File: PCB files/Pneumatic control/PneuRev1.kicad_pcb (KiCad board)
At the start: 2 copper layers, 145.7 x 92.9 mm, 52 parts, among them J1 SIG_IN, J2 BATT_IN, J3 PNEU, U1 uA7824, U2 OP279, U3 OP279, U4 OP279, U5 OP279, U6 OP279, U7 OP279, U8 OP07

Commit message: 2/4/2019
-Finished board routing
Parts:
- moved J2 74.6 mm to (162.6, 68.8), turned to 0 degrees
- moved R40 63.4 mm to (157.7, 71.6), turned to 90 degrees
- moved D1 50.2 mm to (152.8, 69.5)
- moved R39 38.4 mm to (105.4, 72.0)
- moved R38 32.1 mm to (105.4, 76.4), turned to 270 degrees
- moved R19 30.1 mm to (111.6, 131.9), turned to 0 degrees
- moved U8 28.6 mm to (118.1, 77.1)
- moved R37 28.0 mm to (110.6, 82.9)
- moved R21 25.2 mm to (146.4, 132.7), turned to 0 degrees
- moved R1 22.8 mm to (111.1, 107.8)
- moved R24 21.7 mm to (140.7, 125.3), turned to 270 degrees
- moved R29 20.9 mm to (181.9, 132.1), turned to 0 degrees
- moved R11 20.8 mm to (182.7, 106.5)
- moved R3 20.8 mm to (146.1, 106.7)
- moved R22 19.9 mm to (106.8, 125.6)
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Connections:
- U2 pad 1: Net-(J1-Pad1) -> /PNU1
- U2 pad 2: GND -> Net-(R4-Pad1)
- U2 pad 3: /IN2 -> Net-(J1-Pad1)
- U2 pad 4: Net-(R5-Pad1) -> GND
- U2 pad 5: /PNU2 -> /IN2
- U2 pad 6: Net-(U1-Pad3) -> Net-(R5-Pad1)
- U2 pad 7: /PNU1 -> /PNU2
- U2 pad 8: Net-(R4-Pad1) -> Net-(U1-Pad3)
- U3 pad 1: /IN3 -> /PNU3
- U3 pad 2: GND -> Net-(R6-Pad1)
- U3 pad 3: /IN4 -> /IN3
- U3 pad 4: Net-(R13-Pad1) -> GND
- U3 pad 5: /PNU4 -> /IN4
- U3 pad 6: Net-(U1-Pad3) -> Net-(R13-Pad1)
- U3 pad 7: /PNU3 -> /PNU4
- U3 pad 8: Net-(R6-Pad1) -> Net-(U1-Pad3)
- U4 pad 1: /IN5 -> /PNU5
- U4 pad 2: GND -> Net-(R14-Pad1)
- U4 pad 3: /IN6 -> /IN5
- U4 pad 4: Net-(R15-Pad1) -> GND
- U4 pad 5: /PNU6 -> /IN6
- U4 pad 6: Net-(U2-Pad6) -> Net-(R15-Pad1)
- U4 pad 7: /PNU5 -> /PNU6
- U4 pad 8: Net-(R14-Pad1) -> Net-(U1-Pad3)
- U5 pad 1: /IN7 -> /PNU7
- U5 pad 2: GND -> Net-(R22-Pad1)
- U5 pad 3: /IN8 -> /IN7
- U5 pad 4: Net-(R23-Pad1) -> GND
- U5 pad 5: /PNU8 -> /IN8
- U5 pad 6: Net-(U1-Pad3) -> Net-(R23-Pad1)
- U5 pad 7: /PNU7 -> /PNU8
- U5 pad 8: Net-(R22-Pad1) -> Net-(U1-Pad3)
- U6 pad 1: /IN9 -> /PNU9
- U6 pad 2: GND -> Net-(R24-Pad1)
- U6 pad 3: /IN10 -> /IN9
- U6 pad 4: Net-(R31-Pad1) -> GND
- U6 pad 5: /PNU10 -> /IN10
- U6 pad 6: Net-(U1-Pad3) -> Net-(R31-Pad1)
- U6 pad 7: /PNU9 -> /PNU10
- U6 pad 8: Net-(R24-Pad1) -> Net-(U1-Pad3)
- U7 pad 1: /IN11 -> /PNU11
- U7 pad 2: GND -> Net-(R32-Pad1)
- U7 pad 3: /IN12 -> /IN11
- U7 pad 4: Net-(R33-Pad1) -> GND
- U7 pad 5: /PNU12 -> /IN12
- U7 pad 6: Net-(U2-Pad6) -> Net-(R33-Pad1)
- U7 pad 7: /PNU11 -> /PNU12
- U7 pad 8: Net-(R32-Pad1) -> Net-(U1-Pad3)
- U8 pad 1: /IN13 -> /PNU13
- U8 pad 2: GND -> Net-(R38-Pad1)
- U8 pad 3: Net-(U8-Pad3) -> /IN13
- U8 pad 4: Net-(U8-Pad4) -> GND
- U8 pad 6: Net-(U1-Pad3) -> Net-(U8-Pad6)
- U8 pad 7: /PNU13 -> Net-(U8-Pad7)
- U8 pad 8: Net-(R38-Pad1) -> Net-(U1-Pad3)
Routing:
- net Net-(U1-Pad3): track 0.00 -> 249.5 mm, vias 0 -> 10
- net /IN6: track 0.00 -> 136.3 mm, vias 0 -> 4
- net /IN12: track 0.00 -> 135.3 mm, vias 0 -> 2
- net /PNU7: track 0.00 -> 130.8 mm, vias 0 -> 4
- net /PNU1: track 0.00 -> 127.3 mm, vias 0 -> 2
- net /PNU8: track 0.00 -> 123.8 mm, vias 0 -> 4
- net /IN11: track 0.00 -> 123.0 mm, vias 0 -> 2
- net /PNU2: track 0.00 -> 122.8 mm, vias 0 -> 4
- net /IN5: track 0.00 -> 122.3 mm, vias 0 -> 3
- net /PNU13: track 0.00 -> 116.6 mm, vias 0 -> 2
- net /PNU5: track 0.00 -> 104.8 mm, vias 0 -> 2
- net /PNU9: track 0.00 -> 101.6 mm, vias 0 -> 4
- net /IN4: track 0.00 -> 98.6 mm, vias 0 -> 4
- net /IN10: track 0.00 -> 94.6 mm, vias 0 -> 4
- net /PNU10: track 0.00 -> 92.6 mm, vias 0 -> 4
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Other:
- board size 145.7 x 92.9 mm -> 135.4 x 77.3 mm

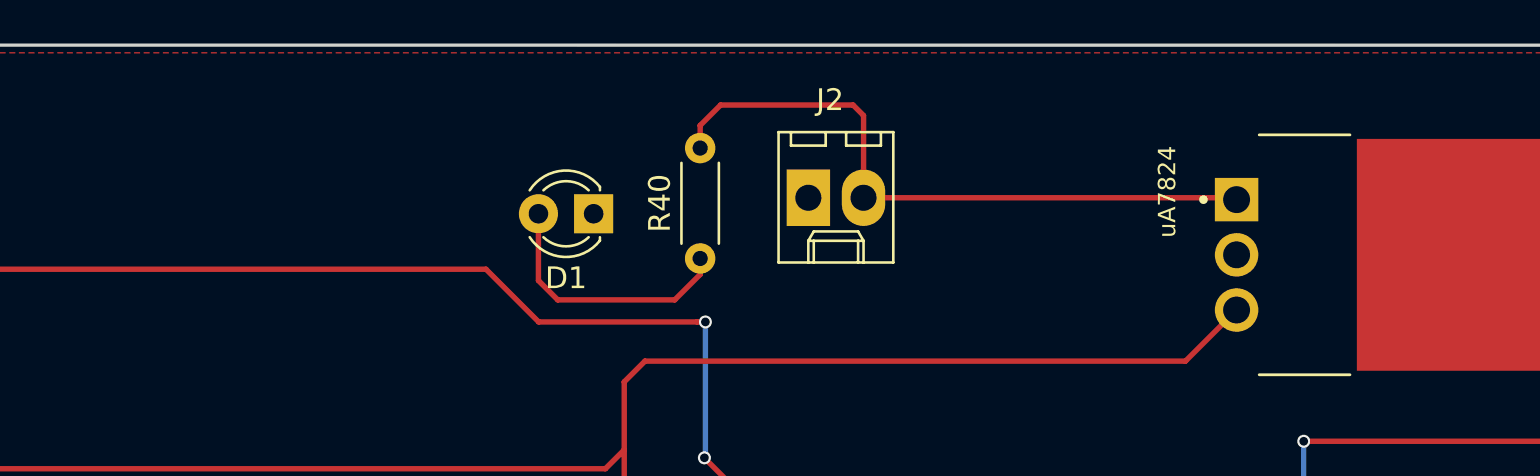
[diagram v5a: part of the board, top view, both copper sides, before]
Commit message: 2/10/2019
-Changed LED resistor to 1.5k
-Set BATT connector to a JST
-Found 383 ohm resistor to replace 390 ohm
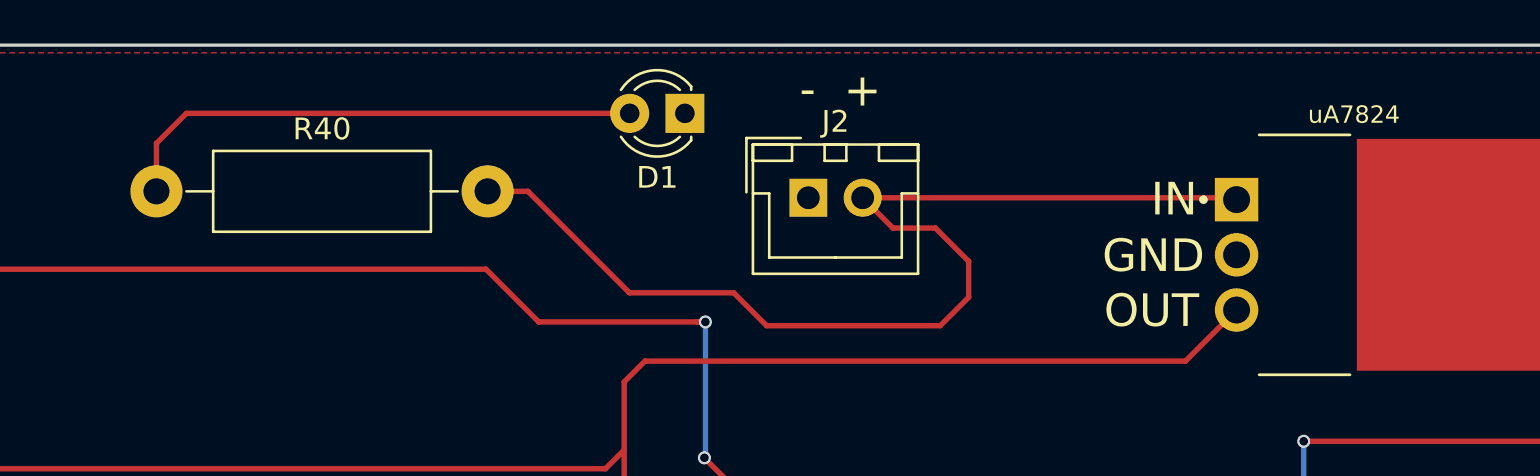
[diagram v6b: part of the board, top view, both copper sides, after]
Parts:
- J2: footprint Connectors_Molex:Molex_KK-6410-02_02x2.54mm_Straight -> Connectors_JST:JST_XH_B02B-XH-A_02x2.50mm_Straight
- R40: value 3k -> 1k5; footprint Resistors_THT:R_Axial_DIN0204_L3.6mm_D1.6mm_P5.08mm_Horizontal -> Resistors_THT:R_Axial_DIN0411_L9.9mm_D3.6mm_P15.24mm_Horizontal
- moved R40 25.2 mm to (132.6, 68.5), turned to 0 degrees
- moved D1 6.24 mm to (157.0, 64.9)
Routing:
- net Net-(J2-Pad2): track 30.9 -> 51.0 mm
- net Net-(D1-Pad2): track 12.1 -> 24.6 mm
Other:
- board text added: "+"
- board text added: "-"
- board text added: "GND"
- board text added: "IN"
- board text added: "OUT"

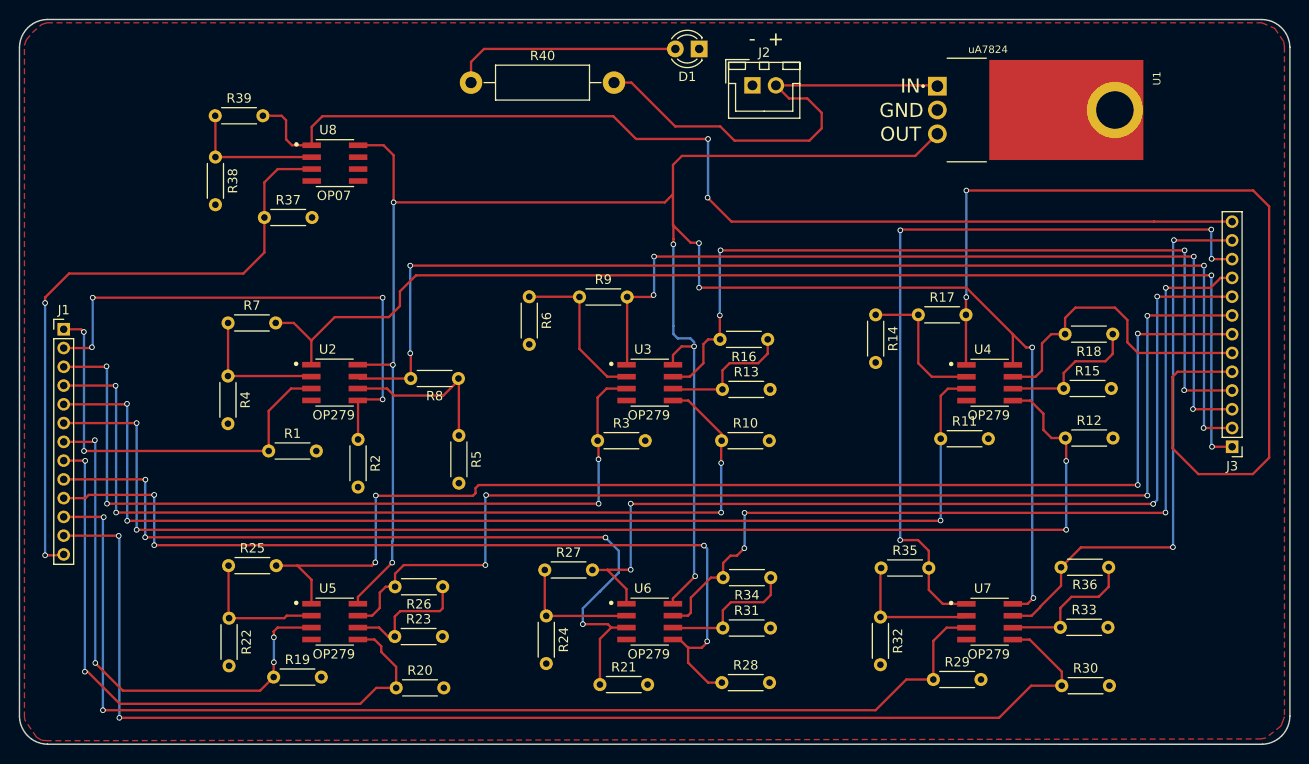
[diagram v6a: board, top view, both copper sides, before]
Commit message: 2/21/2019
-Selected capacitor footprint
-Generated netlist
-Began re-routing board
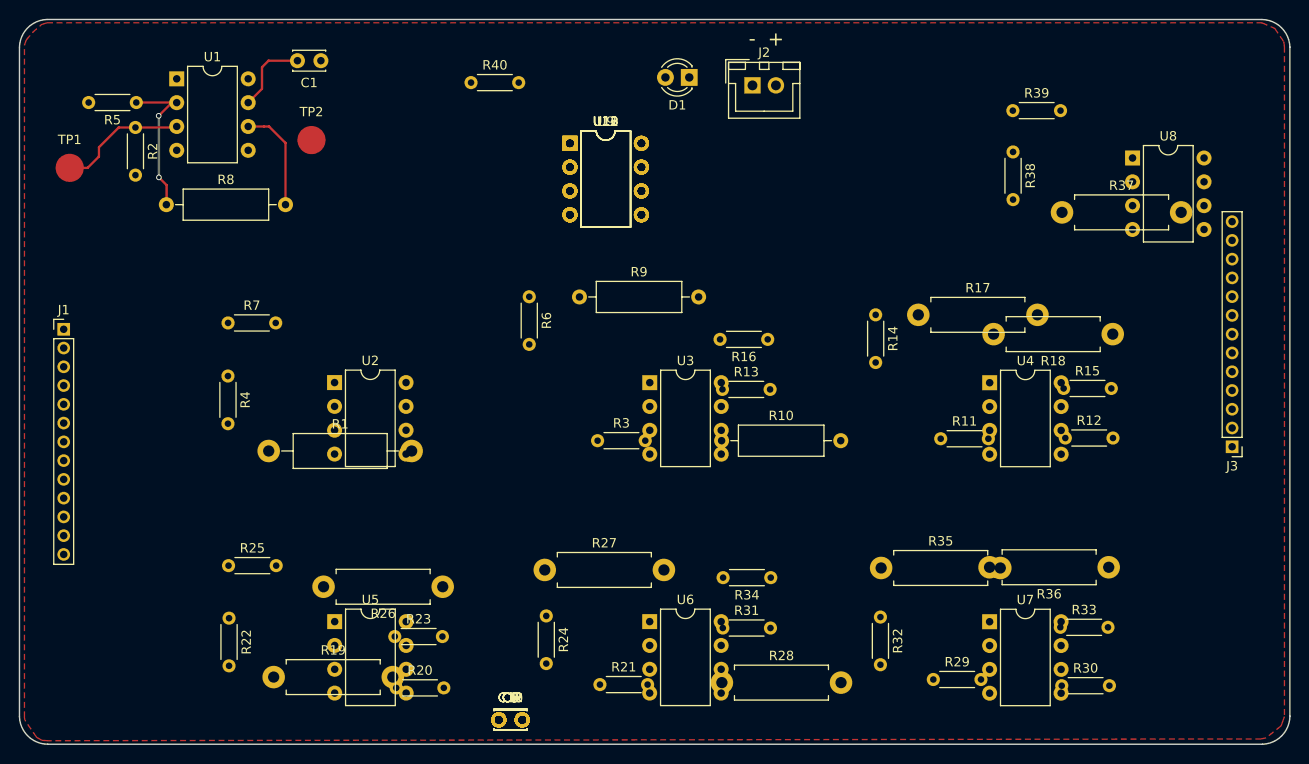
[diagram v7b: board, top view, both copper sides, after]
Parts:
- added C1: 1uF, Capacitors_THT:C_Disc_D3.4mm_W2.1mm_P2.50mm, F.Cu at (116.6, 66.2)
- added C10, C11, C12, C13, C2, C3, C4, C5, C6, C7, C8, C9: 1uF, Capacitors_THT:C_Disc_D3.4mm_W2.1mm_P2.50mm, F.Cu at (135.6, 136.4)
- added TP1: TEST, Measurement_Points:Measurement_Point_Round-SMD-Pad_Big, F.Cu at (89.9, 77.6)
- added TP2: TEST, Measurement_Points:Measurement_Point_Round-SMD-Pad_Big, F.Cu at (115.6, 74.6)
- added U10, U11, U12, U13, U9: OPA551, Housings_DIP:DIP-8_W7.62mm, F.Cu at (143.2, 75.0)
- R1: value 1k -> 3k; footprint Resistors_THT:R_Axial_DIN0204_L3.6mm_D1.6mm_P5.08mm_Horizontal -> Resistors_THT:R_Axial_DIN0411_L9.9mm_D3.6mm_P15.24mm_Horizontal
- R10: value 1k -> 4k; footprint Resistors_THT:R_Axial_DIN0204_L3.6mm_D1.6mm_P5.08mm_Horizontal -> Resistors_THT:R_Axial_DIN0309_L9.0mm_D3.2mm_P12.70mm_Horizontal
- R13, R14, R15, R22, R23, R24, R31, R32, R33, R38, R4, R5, R6: value 100 -> 1k
- R16, R25, R34, R39, R7: value 380 -> 1k
- R17, R18, R26, R27, R35, R36: value 380 -> 4k; footprint Resistors_THT:R_Axial_DIN0204_L3.6mm_D1.6mm_P5.08mm_Horizontal -> Resistors_THT:R_Axial_DIN0411_L9.9mm_D3.6mm_P12.70mm_Horizontal
- R19, R28, R37: value 1k -> 4k; footprint Resistors_THT:R_Axial_DIN0204_L3.6mm_D1.6mm_P5.08mm_Horizontal -> Resistors_THT:R_Axial_DIN0411_L9.9mm_D3.6mm_P12.70mm_Horizontal
- R40: value 1k5 -> 4k; footprint Resistors_THT:R_Axial_DIN0411_L9.9mm_D3.6mm_P15.24mm_Horizontal -> Resistors_THT:R_Axial_DIN0204_L3.6mm_D1.6mm_P5.08mm_Horizontal
- R8, R9: value 380 -> 4k; footprint Resistors_THT:R_Axial_DIN0204_L3.6mm_D1.6mm_P5.08mm_Horizontal -> Resistors_THT:R_Axial_DIN0309_L9.0mm_D3.2mm_P12.70mm_Horizontal
- U1: value uA7824 -> OPA551; footprint ua7824:TO254P1651X1067X470-3 -> Housings_DIP:DIP-8_W7.62mm
- U2, U3, U4, U5, U6, U7: value OP279 -> OPA551; footprint dualopamp:SOIC127P600X175-8N -> Housings_DIP:DIP-8_W7.62mm
- U8: value OP07 -> OPA551; footprint dualopamp:SOIC127P600X175-8N -> Housings_DIP:DIP-8_W7.62mm
- moved R37 85.0 mm to (195.6, 82.3)
- moved R38 85.0 mm to (190.4, 75.9)
- moved R39 85.0 mm to (190.4, 71.5)
- moved U8 85.0 mm to (203.2, 76.5)
- moved U1 81.1 mm to (101.3, 68.1), turned to 0 degrees
- moved R5 49.4 mm to (97.0, 70.6), turned to 180 degrees
- moved R2 40.9 mm to (96.9, 73.3)
- moved R8 36.2 mm to (100.2, 81.5), turned to 0 degrees
- moved D1 3.21 mm to (155.9, 67.9)
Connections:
- J2 pad 2: Net-(J2-Pad2) -> Net-(C1-Pad2)
- R1 pad 1: Net-(J1-Pad1) -> Net-(D1-Pad2)
- R1 pad 2: GND -> Net-(C1-Pad2)
- R10 pad 1: /IN4 -> Net-(R10-Pad1)
- R10 pad 2: GND -> /PNU3
- R11 pad 1: /IN5 -> /IN4
- R12 pad 1: /IN6 -> /IN5
- R13 pad 1: Net-(R13-Pad1) -> /IN6
- R16 pad 1: Net-(R13-Pad1) -> Net-(R16-Pad1)
- R16 pad 2: /PNU4 -> GND
- R17 pad 2: /PNU5 -> /PNU4
- R18 pad 2: /PNU6 -> /PNU5
- R19 pad 1: /IN7 -> Net-(R16-Pad1)
- R19 pad 2: GND -> /PNU6
- R2 pad 1: /IN2 -> Net-(J1-Pad1)
- R20 pad 1: /IN8 -> /IN7
- R21 pad 1: /IN9 -> /IN8
- R22 pad 1: Net-(R22-Pad1) -> /IN9
- R25 pad 1: Net-(R22-Pad1) -> Net-(R25-Pad1)
- R25 pad 2: /PNU7 -> GND
- R26 pad 2: /PNU8 -> /PNU7
- R27 pad 2: /PNU9 -> /PNU8
- R28 pad 1: /IN10 -> Net-(R25-Pad1)
- R28 pad 2: GND -> /PNU9
- R29 pad 1: /IN11 -> /IN10
- R3 pad 1: /IN3 -> /IN2
- R30 pad 1: /IN12 -> /IN11
- R31 pad 1: Net-(R31-Pad1) -> /IN12
- R34 pad 1: Net-(R31-Pad1) -> Net-(R34-Pad1)
- R34 pad 2: /PNU10 -> GND
- R35 pad 2: /PNU11 -> /PNU10
- R36 pad 2: /PNU12 -> /PNU11
- R37 pad 1: /IN13 -> Net-(R34-Pad1)
- R37 pad 2: GND -> /PNU12
- R38 pad 1: Net-(R38-Pad1) -> /IN13
- R39 pad 1: Net-(R38-Pad1) -> Net-(R39-Pad1)
- R39 pad 2: /PNU13 -> GND
- R4 pad 1: Net-(R4-Pad1) -> /IN3
- R40 pad 1: Net-(D1-Pad2) -> Net-(R39-Pad1)
- R40 pad 2: Net-(J2-Pad2) -> /PNU13
- R7 pad 1: Net-(R4-Pad1) -> Net-(R10-Pad1)
- R7 pad 2: /PNU1 -> GND
- R8 pad 2: /PNU2 -> /PNU1
- R9 pad 2: /PNU3 -> /PNU2
- U1 pad 1: Net-(J2-Pad2) -> Net-(U1-Pad1)
- U1 pad 2: GND -> Net-(R5-Pad1)
- U1 pad 3: Net-(U1-Pad3) -> Net-(J1-Pad1)
- U1 pad 4: (no net) -> GND
- U2 pad 1: /PNU1 -> Net-(U2-Pad1)
- U2 pad 2: Net-(R4-Pad1) -> Net-(R6-Pad1)
- U2 pad 3: Net-(J1-Pad1) -> /IN2
- U2 pad 5: /IN2 -> Net-(U2-Pad5)
- U2 pad 6: Net-(R5-Pad1) -> /PNU2
- U2 pad 7: /PNU2 -> Net-(C1-Pad2)
- U2 pad 8: Net-(U1-Pad3) -> Net-(U2-Pad8)
- U3 pad 1: /PNU3 -> Net-(U3-Pad1)
- U3 pad 2: Net-(R6-Pad1) -> Net-(R10-Pad1)
- U3 pad 5: /IN4 -> Net-(U3-Pad5)
- U3 pad 6: Net-(R13-Pad1) -> /PNU3
- U3 pad 7: /PNU4 -> Net-(C1-Pad2)
- U3 pad 8: Net-(U1-Pad3) -> Net-(U3-Pad8)
- U4 pad 1: /PNU5 -> Net-(U4-Pad1)
- U4 pad 3: /IN5 -> /IN4
- U4 pad 5: /IN6 -> Net-(U4-Pad5)
- U4 pad 6: Net-(R15-Pad1) -> /PNU4
- U4 pad 7: /PNU6 -> Net-(C1-Pad2)
- U4 pad 8: Net-(U1-Pad3) -> Net-(U4-Pad8)
- U5 pad 1: /PNU7 -> Net-(U5-Pad1)
- U5 pad 2: Net-(R22-Pad1) -> Net-(R15-Pad1)
- U5 pad 3: /IN7 -> /IN5
- U5 pad 5: /IN8 -> Net-(U5-Pad5)
- U5 pad 6: Net-(R23-Pad1) -> /PNU5
- U5 pad 7: /PNU8 -> Net-(C1-Pad2)
- U5 pad 8: Net-(U1-Pad3) -> Net-(U5-Pad8)
- U6 pad 1: /PNU9 -> Net-(U6-Pad1)
- U6 pad 2: Net-(R24-Pad1) -> Net-(R16-Pad1)
- U6 pad 3: /IN9 -> /IN6
- U6 pad 5: /IN10 -> Net-(U6-Pad5)
- U6 pad 6: Net-(R31-Pad1) -> /PNU6
- U6 pad 7: /PNU10 -> Net-(C1-Pad2)
- U6 pad 8: Net-(U1-Pad3) -> Net-(U6-Pad8)
- U7 pad 1: /PNU11 -> Net-(U7-Pad1)
- U7 pad 2: Net-(R32-Pad1) -> Net-(R23-Pad1)
- U7 pad 3: /IN11 -> /IN7
- U7 pad 5: /IN12 -> Net-(U7-Pad5)
- U7 pad 6: Net-(R33-Pad1) -> /PNU7
- U7 pad 7: /PNU12 -> Net-(C1-Pad2)
- U7 pad 8: Net-(U1-Pad3) -> Net-(U7-Pad8)
- U8 pad 1: /PNU13 -> Net-(U8-Pad1)
- U8 pad 2: Net-(R38-Pad1) -> Net-(R24-Pad1)
- U8 pad 3: /IN13 -> /IN8
- U8 pad 6: Net-(U8-Pad6) -> /PNU8
- U8 pad 7: Net-(U8-Pad7) -> Net-(C1-Pad2)
- U8 pad 8: Net-(U1-Pad3) -> Net-(U8-Pad8)
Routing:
- net Net-(U1-Pad3): track 249.5 -> 0.00 mm, vias 10 -> 0
- net /IN6: track 136.3 -> 0.00 mm, vias 4 -> 0
- net /IN12: track 135.3 -> 0.00 mm, vias 2 -> 0
- net /PNU7: track 130.8 -> 0.00 mm, vias 4 -> 0
- net /PNU8: track 123.8 -> 0.00 mm, vias 4 -> 0
- net /IN11: track 123.0 -> 0.00 mm, vias 2 -> 0
- net /PNU2: track 122.8 -> 0.00 mm, vias 4 -> 0
- net /IN5: track 122.3 -> 0.00 mm, vias 3 -> 0
- net /PNU13: track 116.6 -> 0.00 mm, vias 2 -> 0
- net /PNU1: track 127.3 -> 11.3 mm, vias 2 -> 0
- net /PNU5: track 104.8 -> 0.00 mm, vias 2 -> 0
- net /PNU9: track 101.6 -> 0.00 mm, vias 4 -> 0
- net /IN4: track 98.6 -> 0.00 mm, vias 4 -> 0
- net /IN10: track 94.6 -> 0.00 mm, vias 4 -> 0
- net /PNU10: track 92.6 -> 0.00 mm, vias 4 -> 0
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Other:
- board text removed: "GND"
- board text removed: "IN"
- board text removed: "OUT"
